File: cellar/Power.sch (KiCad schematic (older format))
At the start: 29 parts

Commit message: Schematic done, pending review.
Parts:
- removed C? (x2): 22uF/6.3V, symbol Device:C
- added C14, C15: 22uF/6.3V, symbol Device:CP
- added MH1, MH2, MH3, MH4: MountingHole_Pad, MountingHole:MountingHole_3.2mm_M3_Pad_Via, symbol Mechanical:MountingHole_Pad
- D1, D2, D3: renamed from D?; Farnell (none) -> 1863724; Ref (none) -> SBR160S23-7
- R2: renamed from R?; value 37.4k -> 22.1k
- gave numbers to parts that had none: 23
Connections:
- wire segments 103 -> 112

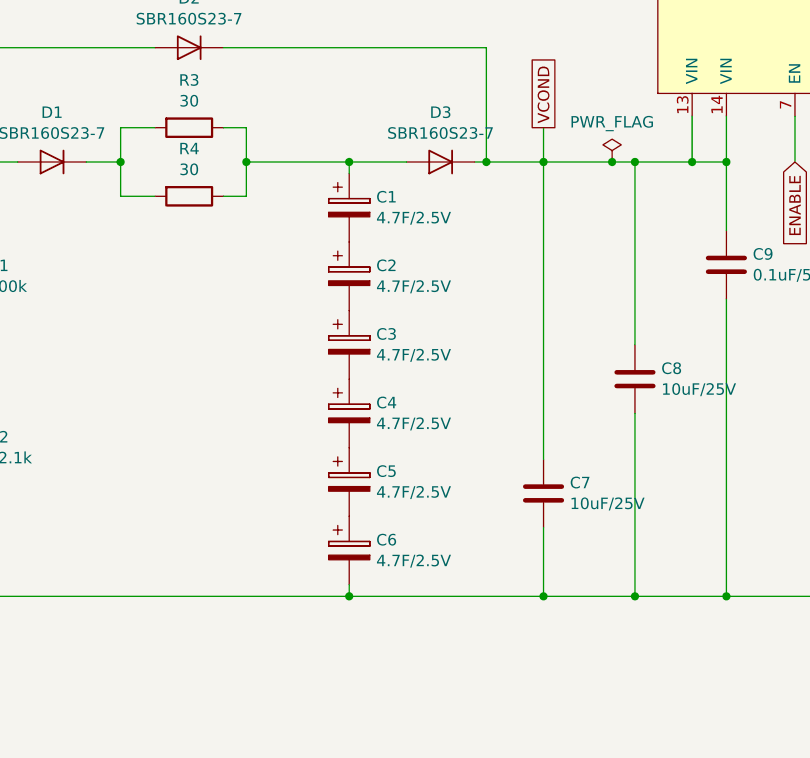
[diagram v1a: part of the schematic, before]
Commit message: Changed supercap ref, updated some footprints.
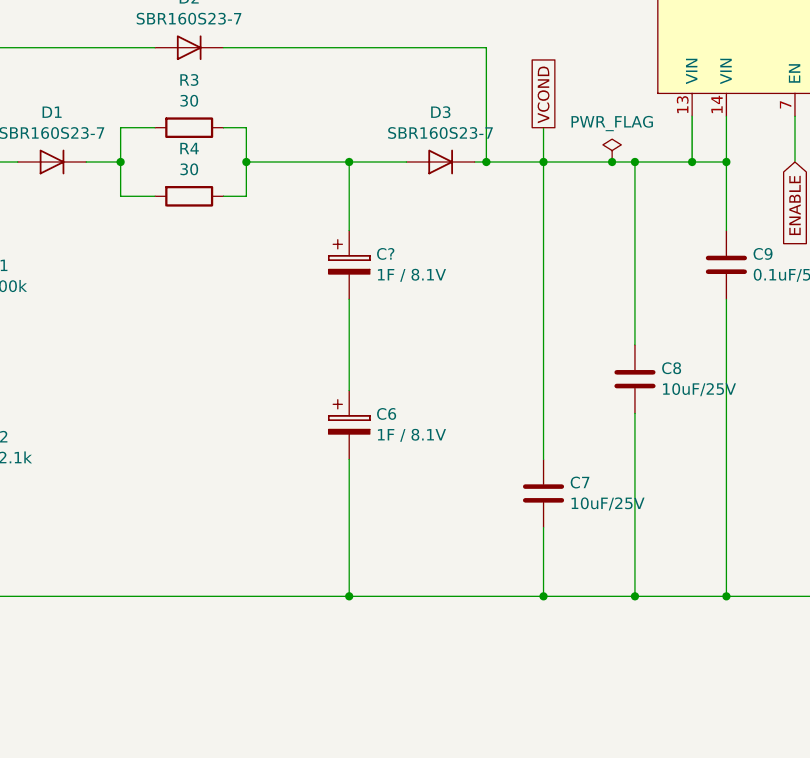
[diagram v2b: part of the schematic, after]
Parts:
- removed C1, C2, C3, C4, C5: 4.7F/2.5V, symbol Device:CP
- added C?: 1F / 8.1V, Capacitors:SCMR22J105SRBA0_vertical, symbol Device:CP
- C6: value 4.7F/2.5V -> 1F / 8.1V; footprint (none) -> Capacitors:SCMR22J105SRBA0_vertical; Farnell (none) -> 2856949; Ref (none) -> SCMR22J105SRBA0
- L1: footprint (none) -> Inductors:L_7.1x6.5_H3; Farnell (none) -> 2215610; Ref (none) -> SPM6530T-1R5M100
- R3, R4: Farnell (none) -> 2331667; Ref (none) -> SMW530RJT
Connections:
- wire segments 112 -> 113
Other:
- moved on the sheet: C6
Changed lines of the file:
@@
 F 0 "L1" H 8850 2315 50  0000 C CNN
 F 1 "1.5uH" H 8850 2224 50  0000 C CNN
-F 2 "" H 8850 2100 50  0001 C CNN
+F 2 "Inductors:L_7.1x6.5_H3" H 8850 2100 50  0001 C CNN
 F 3 "" H 8850 2100 50  0001 C CNN
+F 4 "2215610" H 8850 2100 50  0001 C CNN "Farnell"
+F 5 "SPM6530T-1R5M100" H 8850 2100 50  0001 C CNN "Ref"
 	1    8850 2100
 	1    0    0    -1
@@
 	10000 3600 10000 3750
 $Comp
-L Device:CP C1
-U 1 1 5BCFB2DD
-P 3750 1900
-F 0 "C1" H 3868 1946 50  0000 L CNN
-F 1 "4.7F/2.5V" H 3868 1855 50  0000 L CNN
-F 2 "" H 3788 1750 50  0001 C CNN
-F 3 "~" H 3750 1900 50  0001 C CNN
-	1    3750 1900
-	1    0    0    -1
-$EndComp
-$Comp
-L Device:CP C2
-U 1 1 5BCFB408
-P 3750 2200
-F 0 "C2" H 3868 2246 50  0000 L CNN
-F 1 "4.7F/2.5V" H 3868 2155 50  0000 L CNN
-F 2 "" H 3788 2050 50  0001 C CNN
-F 3 "~" H 3750 2200 50  0001 C CNN
-	1    3750 2200
-	1    0    0    -1
-$EndComp
-$Comp
-L Device:CP C3
-U 1 1 5BCFB550
-P 3750 2500
-F 0 "C3" H 3868 2546 50  0000 L CNN
-F 1 "4.7F/2.5V" H 3868 2455 50  0000 L CNN
-F 2 "" H 3788 2350 50  0001 C CNN
-F 3 "~" H 3750 2500 50  0001 C CNN
-	1    3750 2500
-	1    0    0    -1
-$EndComp
-$Comp
-L Device:CP C4
-U 1 1 5BCFB58E
-P 3750 2800
-F 0 "C4" H 3868 2846 50  0000 L CNN
-F 1 "4.7F/2.5V" H 3868 2755 50  0000 L CNN
-F 2 "" H 3788 2650 50  0001 C CNN
-F 3 "~" H 3750 2800 50  0001 C CNN
-	1    3750 2800
-	1    0    0    -1
-$EndComp
-$Comp
-L Device:CP C5
-U 1 1 5BCFB5CA
-P 3750 3100
-F 0 "C5" H 3868 3146 50  0000 L CNN
-F 1 "4.7F/2.5V" H 3868 3055 50  0000 L CNN
-F 2 "" H 3788 2950 50  0001 C CNN
-F 3 "~" H 3750 3100 50  0001 C CNN
-	1    3750 3100
-	1    0    0    -1
-$EndComp
-$Comp
 L Device:CP C6
 U 1 1 5BCFB957
-P 3750 3400
-F 0 "C6" H 3868 3446 50  0000 L CNN
-F 1 "4.7F/2.5V" H 3868 3355 50  0000 L CNN
-F 2 "" H 3788 3250 50  0001 C CNN
-F 3 "~" H 3750 3400 50  0001 C CNN
-	1    3750 3400
+P 3750 2850
+F 0 "C6" H 3868 2896 50  0000 L CNN
+F 1 "1F / 8.1V" H 3868 2805 50  0000 L CNN
+F 2 "Capacitors:SCMR22J105SRBA0_vertical" H 3788 2700 50  0001 C CNN
+F 3 "~" H 3750 2850 50  0001 C CNN
+F 4 "2856949" H 3750 2850 50  0001 C CNN "Farnell"
+F 5 "SCMR22J105SRBA0" H 3750 2850 50  0001 C CNN "Ref"
+	1    3750 2850
 	1    0    0    -1
 $EndComp
@@
 F 2 "" V 2980 1550 50  0001 C CNN
 F 3 "~" H 3050 1550 50  0001 C CNN
+F 4 "2331667" H 3050 1550 50  0001 C CNN "Farnell"
+F 5 "SMW530RJT" H 3050 1550 50  0001 C CNN "Ref"
 	1    3050 1550
-	0    1    1    0
-$EndComp
-$Comp
-L Device:R R4
-U 1 1 5BCFCCFA
-P 3050 1850
-F 0 "R4" V 2843 1850 50  0000 C CNN
-F 1 "30" V 2934 1850 50  0000 C CNN
-F 2 "" V 2980 1850 50  0001 C CNN
-F 3 "~" H 3050 1850 50  0001 C CNN
-	1    3050 1850
 	0    1    1    0
 $EndComp
@@
 	4000 1700 3750 1700
 Wire Wire Line
-	3750 1700 3750 1750
-Wire Wire Line
-	3750 3550 3750 3600
+	3750 3000 3750 3600
 Wire Wire Line
 	3750 3600 4600 3600
@@
 Wire Wire Line
 	4900 1700 4600 1700
+$Comp
+L Device:R R4
+U 1 1 5BECFA96
+P 3050 1850
+F 0 "R4" V 2843 1850 50  0000 C CNN
+F 1 "30" V 2934 1850 50  0000 C CNN
+F 2 "" V 2980 1850 50  0001 C CNN
+F 3 "~" H 3050 1850 50  0001 C CNN
+F 4 "2331667" H 3050 1850 50  0001 C CNN "Farnell"
+F 5 "SMW530RJT" H 3050 1850 50  0001 C CNN "Ref"
+	1    3050 1850
+	0    1    1    0
+$EndComp
+$Comp
+L Device:CP C?
+U 1 1 5BED7949
+P 3750 2150
+F 0 "C?" H 3868 2196 50  0000 L CNN
+F 1 "1F / 8.1V" H 3868 2105 50  0000 L CNN
+F 2 "Capacitors:SCMR22J105SRBA0_vertical" H 3788 2000 50  0001 C CNN
+F 3 "~" H 3750 2150 50  0001 C CNN
+F 4 "2856949" H 3750 2150 50  0001 C CNN "Farnell"
+F 5 "SCMR22J105SRBA0" H 3750 2150 50  0001 C CNN "Ref"
+	1    3750 2150
+	1    0    0    -1
+$EndComp
+Wire Wire Line
+	3750 2300 3750 2700
+Wire Wire Line
+	3750 1700 3750 2000
 $EndSCHEMATC

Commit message: Replaced wirepads by phoenix connectors.
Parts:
- removed W1: POWER +, Pads:wirepad_hole_3x1.5mm, symbol pads:WirePad
- removed W2: GND, Pads:wirepad_hole_3x1.5mm, symbol pads:WirePad
- C10: renamed from C14; footprint (none) -> Capacitor_Tantalum_SMD:CP_EIA-3216-10_Kemet-I_Pad1.58x1.35mm_HandSolder
- C11: renamed from C15; footprint (none) -> Capacitor_Tantalum_SMD:CP_EIA-3216-10_Kemet-I_Pad1.58x1.35mm_HandSolder
- C3: renamed from C7; footprint (none) -> Capacitor_SMD:C_0805_2012Metric_Pad1.15x1.40mm_HandSolder
- C4: renamed from C8; footprint (none) -> Capacitor_SMD:C_0805_2012Metric_Pad1.15x1.40mm_HandSolder
- C5: renamed from C9; footprint (none) -> Capacitor_SMD:C_0603_1608Metric_Pad1.05x0.95mm_HandSolder
- C6: renamed from C10; footprint (none) -> Capacitor_SMD:C_0805_2012Metric_Pad1.15x1.40mm_HandSolder
- C7: renamed from C11; footprint (none) -> Capacitor_SMD:C_0603_1608Metric_Pad1.05x0.95mm_HandSolder
- C8: renamed from C12; footprint (none) -> Capacitor_SMD:C_0603_1608Metric_Pad1.05x0.95mm_HandSolder
- C9: renamed from C13; footprint (none) -> Capacitor_SMD:C_0603_1608Metric_Pad1.05x0.95mm_HandSolder
- U1: Farnell (none) -> 2361244; Ref (none) -> TPS54625PWP
- gave numbers to parts that had none: 1
- renumbered C6 to C2
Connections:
- wire segments 113 -> 106
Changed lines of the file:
@@
 F 2 "TexasInstruments:HTSSOP-14-PWP" H 6850 800 50  0001 C CNN
 F 3 "http://www.ti.com/lit/ds/symlink/tps54625.pdf" H 6850 800 50  0001 C CNN
+F 4 "2361244" H 6850 800 50  0001 C CNN "Farnell"
+F 5 "TPS54625PWP" H 6850 800 50  0001 C CNN "Ref"
 	1    6850 800
 	1    0    0    -1
 $EndComp
 $Comp
-L Device:C C9
+L Device:C C5
 U 1 1 5BCDE8A2
 P 5400 2150
-F 0 "C9" H 5515 2196 50  0000 L CNN
+F 0 "C5" H 5515 2196 50  0000 L CNN
 F 1 "0.1uF/50V" H 5515 2105 50  0000 L CNN
-F 2 "" H 5438 2000 50  0001 C CNN
+F 2 "Capacitor_SMD:C_0603_1608Metric_Pad1.05x0.95mm_HandSolder" H 5438 2000 50  0001 C CNN
 F 3 "~" H 5400 2150 50  0001 C CNN
 	1    5400 2150
@@
 $EndComp
 $Comp
-L Device:C C8
+L Device:C C4
 U 1 1 5BCDE8C0
 P 5000 2650
-F 0 "C8" H 5115 2696 50  0000 L CNN
+F 0 "C4" H 5115 2696 50  0000 L CNN
 F 1 "10uF/25V" H 5115 2605 50  0000 L CNN
-F 2 "" H 5038 2500 50  0001 C CNN
+F 2 "Capacitor_SMD:C_0805_2012Metric_Pad1.15x1.40mm_HandSolder" H 5038 2500 50  0001 C CNN
 F 3 "~" H 5000 2650 50  0001 C CNN
 	1    5000 2650
@@
 $EndComp
 $Comp
-L Device:C C7
+L Device:C C3
 U 1 1 5BCDE8FA
 P 4600 3150
-F 0 "C7" H 4715 3196 50  0000 L CNN
+F 0 "C3" H 4715 3196 50  0000 L CNN
 F 1 "10uF/25V" H 4715 3105 50  0000 L CNN
-F 2 "" H 4638 3000 50  0001 C CNN
+F 2 "Capacitor_SMD:C_0805_2012Metric_Pad1.15x1.40mm_HandSolder" H 4638 3000 50  0001 C CNN
 F 3 "~" H 4600 3150 50  0001 C CNN
 	1    4600 3150
@@
 $EndComp
 $Comp
-L power:GND #PWR09
+L power:GND #PWR011
 U 1 1 5BCDE96A
 P 7050 3750
-F 0 "#PWR09" H 7050 3500 50  0001 C CNN
+F 0 "#PWR011" H 7050 3500 50  0001 C CNN
 F 1 "GND" H 7055 3577 50  0000 C CNN
 F 2 "" H 7050 3750 50  0001 C CNN
@@
 	5000 1700 5000 2500
 Connection ~ 5250 1700
-Wire Wire Line
-	5000 1700 4900 1700
 Wire Wire Line
 	4600 1700 4600 3000
@@
 $EndComp
 $Comp
-L Device:C C10
+L Device:C C6
 U 1 1 5BCDF240
 P 6150 2700
-F 0 "C10" H 6265 2746 50  0000 L CNN
+F 0 "C6" H 6265 2746 50  0000 L CNN
 F 1 "1uF/25V" H 6265 2655 50  0000 L CNN
-F 2 "" H 6188 2550 50  0001 C CNN
+F 2 "Capacitor_SMD:C_0805_2012Metric_Pad1.15x1.40mm_HandSolder" H 6188 2550 50  0001 C CNN
 F 3 "~" H 6150 2700 50  0001 C CNN
 	1    6150 2700
@@
 $EndComp
 $Comp
-L Device:C C11
+L Device:C C7
 U 1 1 5BCDF284
 P 6450 3200
-F 0 "C11" H 6565 3246 50  0000 L CNN
+F 0 "C7" H 6565 3246 50  0000 L CNN
 F 1 "8200pF/50V" H 6565 3155 50  0000 L CNN
-F 2 "" H 6488 3050 50  0001 C CNN
+F 2 "Capacitor_SMD:C_0603_1608Metric_Pad1.05x0.95mm_HandSolder" H 6488 3050 50  0001 C CNN
 F 3 "~" H 6450 3200 50  0001 C CNN
 	1    6450 3200
@@
 	6450 3600 7050 3600
 $Comp
-L Device:C C12
+L Device:C C8
 U 1 1 5BCE0D07
 P 7950 1750
-F 0 "C12" H 8065 1796 50  0000 L CNN
+F 0 "C8" H 8065 1796 50  0000 L CNN
 F 1 "0.1uF/50V" H 8065 1705 50  0000 L CNN
-F 2 "" H 7988 1600 50  0001 C CNN
+F 2 "Capacitor_SMD:C_0603_1608Metric_Pad1.05x0.95mm_HandSolder" H 7988 1600 50  0001 C CNN
 F 3 "~" H 7950 1750 50  0001 C CNN
 	1    7950 1750
@@
 $EndComp
 $Comp
-L Device:C C13
+L Device:C C9
 U 1 1 5BCE25CA
 P 8150 2600
-F 0 "C13" H 8265 2646 50  0000 L CNN
+F 0 "C9" H 8265 2646 50  0000 L CNN
 F 1 "10pF/50V" H 8265 2555 50  0000 L CNN
-F 2 "" H 8188 2450 50  0001 C CNN
+F 2 "Capacitor_SMD:C_0603_1608Metric_Pad1.05x0.95mm_HandSolder" H 8188 2450 50  0001 C CNN
 F 3 "~" H 8150 2600 50  0001 C CNN
 	1    8150 2600
@@
 	7050 3600 7050 3750
 $Comp
-L power:+5V #PWR011
+L power:+5V #PWR013
 U 1 1 5BCEEFBC
 P 10250 1850
-F 0 "#PWR011" H 10250 1700 50  0001 C CNN
+F 0 "#PWR013" H 10250 1700 50  0001 C CNN
 F 1 "+5V" H 10265 2023 50  0000 C CNN
 F 2 "" H 10250 1850 50  0001 C CNN
@@
 $EndComp
 $Comp
-L power:GND #PWR010
+L power:GND #PWR012
 U 1 1 5BCEF139
 P 10000 3750
-F 0 "#PWR010" H 10000 3500 50  0001 C CNN
+F 0 "#PWR012" H 10000 3500 50  0001 C CNN
 F 1 "GND" H 10005 3577 50  0000 C CNN
 F 2 "" H 10000 3750 50  0001 C CNN
@@
 $EndComp
 $Comp
-L power:GND #PWR07
+L power:GND #PWR09
 U 1 1 5BCEF24E
 P 2100 3750
-F 0 "#PWR07" H 2100 3500 50  0001 C CNN
+F 0 "#PWR09" H 2100 3500 50  0001 C CNN
 F 1 "GND" H 2105 3577 50  0000 C CNN
 F 2 "" H 2100 3750 50  0001 C CNN
@@
 	10000 3600 10000 3750
 $Comp
-L Device:CP C6
+L Device:CP C2
 U 1 1 5BCFB957
 P 3750 2850
-F 0 "C6" H 3868 2896 50  0000 L CNN
+F 0 "C2" H 3868 2896 50  0000 L CNN
 F 1 "1F / 8.1V" H 3868 2805 50  0000 L CNN
 F 2 "Capacitors:SCMR22J105SRBA0_vertical" H 3788 2700 50  0001 C CNN
@@
 	2100 2350 2100 2600
 $Comp
-L power:+12V #PWR06
+L power:+12V #PWR08
 U 1 1 5BD2D830
 P 1800 1450
-F 0 "#PWR06" H 1800 1300 50  0001 C CNN
+F 0 "#PWR08" H 1800 1300 50  0001 C CNN
 F 1 "+12V" H 1815 1623 50  0000 C CNN
 F 2 "" H 1800 1450 50  0001 C CNN
@@
 $EndComp
 Connection ~ 2100 3600
-$Comp
-L pads:WirePad W1
-U 1 1 5BD42CBA
-P 1100 6250
-F 0 "W1" V 885 6181 50  0000 C CNN
-F 1 "POWER +" V 976 6181 50  0000 C CNN
-F 2 "Pads:wirepad_hole_3x1.5mm" H 1100 6250 50  0001 C CNN
-F 3 "" H 1100 6250 50  0001 C CNN
-	1    1100 6250
-	0    1    1    0
-$EndComp
-$Comp
-L pads:WirePad W2
-U 1 1 5BD42E4B
-P 1100 6700
-F 0 "W2" V 885 6631 50  0000 C CNN
-F 1 "GND" V 976 6631 50  0000 C CNN
-F 2 "Pads:wirepad_hole_3x1.5mm" H 1100 6700 50  0001 C CNN
-F 3 "" H 1100 6700 50  0001 C CNN
-	1    1100 6700
-	0    1    1    0
-$EndComp
-Wire Wire Line
-	1100 6250 1350 6250
-Wire Wire Line
-	1600 6250 1600 5950
-Wire Wire Line
-	1100 6700 1350 6700
-Wire Wire Line
-	1600 6700 1600 7000
-$Comp
-L power:+12V #PWR04
-U 1 1 5BD48DD8
-P 1600 5950
-F 0 "#PWR04" H 1600 5800 50  0001 C CNN
-F 1 "+12V" H 1615 6123 50  0000 C CNN
-F 2 "" H 1600 5950 50  0001 C CNN
-F 3 "" H 1600 5950 50  0001 C CNN
-	1    1600 5950
-	1    0    0    -1
-$EndComp
-$Comp
-L power:GND #PWR05
-U 1 1 5BD48E3B
-P 1600 7000
-F 0 "#PWR05" H 1600 6750 50  0001 C CNN
-F 1 "GND" H 1605 6827 50  0000 C CNN
-F 2 "" H 1600 7000 50  0001 C CNN
-F 3 "" H 1600 7000 50  0001 C CNN
-	1    1600 7000
-	1    0    0    -1
-$EndComp
 Connection ~ 4350 1700
 Wire Wire Line
@@
 	3850 6900 3850 7100
 $Comp
-L power:GND #PWR08
+L power:GND #PWR010
 U 1 1 5BE43A97
 P 3850 7100
-F 0 "#PWR08" H 3850 6850 50  0001 C CNN
+F 0 "#PWR010" H 3850 6850 50  0001 C CNN
 F 1 "GND" H 3855 6927 50  0000 C CNN
 F 2 "" H 3850 7100 50  0001 C CNN
@@
 P 9450 3100
 AR Path="/5BE442FC/5BE47BD7" Ref="C?"  Part="1"
-AR Path="/5BCDDEA3/5BE47BD7" Ref="C14"  Part="1"
-F 0 "C14" H 9568 3146 50  0000 L CNN
+AR Path="/5BCDDEA3/5BE47BD7" Ref="C10"  Part="1"
+F 0 "C10" H 9568 3146 50  0000 L CNN
 F 1 "22uF/6.3V" H 9568 3055 50  0000 L CNN
-F 2 "" H 9488 2950 50  0001 C CNN
+F 2 "Capacitor_Tantalum_SMD:CP_EIA-3216-10_Kemet-I_Pad1.58x1.35mm_HandSolder" H 9488 2950 50  0001 C CNN
 F 3 "~" H 9450 3100 50  0001 C CNN
 F 4 "2321204" H 150 -300 50  0001 C CNN "Farnell"
@@
 P 10000 2600
 AR Path="/5BE442FC/5BE4EA38" Ref="C?"  Part="1"
-AR Path="/5BCDDEA3/5BE4EA38" Ref="C15"  Part="1"
-F 0 "C15" H 10118 2646 50  0000 L CNN
+AR Path="/5BCDDEA3/5BE4EA38" Ref="C11"  Part="1"
+F 0 "C11" H 10118 2646 50  0000 L CNN
 F 1 "22uF/6.3V" H 10118 2555 50  0000 L CNN
-F 2 "" H 10038 2450 50  0001 C CNN
+F 2 "Capacitor_Tantalum_SMD:CP_EIA-3216-10_Kemet-I_Pad1.58x1.35mm_HandSolder" H 10038 2450 50  0001 C CNN
 F 3 "~" H 10000 2600 50  0001 C CNN
 F 4 "2321204" H 700 -800 50  0001 C CNN "Farnell"
@@
 Text GLabel 5700 1700 3    50   Input ~ 0
 ENABLE
-$Comp
-L power:PWR_FLAG #FLG0102
-U 1 1 5BE87EF0
-P 1350 6250
-F 0 "#FLG0102" H 1350 6325 50  0001 C CNN
-F 1 "PWR_FLAG" H 1350 6424 50  0000 C CNN
-F 2 "" H 1350 6250 50  0001 C CNN
-F 3 "~" H 1350 6250 50  0001 C CNN
-	1    1350 6250
-	1    0    0    -1
-$EndComp
-Connection ~ 1350 6250
-Wire Wire Line
-	1350 6250 1600 6250
-$Comp
-L power:PWR_FLAG #FLG0103
-U 1 1 5BE87F46
-P 1350 6700
-F 0 "#FLG0103" H 1350 6775 50  0001 C CNN
-F 1 "PWR_FLAG" H 1350 6874 50  0000 C CNN
-F 2 "" H 1350 6700 50  0001 C CNN
-F 3 "~" H 1350 6700 50  0001 C CNN
-	1    1350 6700
-	1    0    0    -1
-$EndComp
-Connection ~ 1350 6700
-Wire Wire Line
-	1350 6700 1600 6700
 Wire Wire Line
 	9450 2100 10000 2100
 $Comp
-L power:PWR_FLAG #FLG0104
+L power:PWR_FLAG #FLG04
 U 1 1 5BE90F84
-P 4900 1700
-F 0 "#FLG0104" H 4900 1775 50  0001 C CNN
-F 1 "PWR_FLAG" H 4900 1874 50  0000 C CNN
-F 2 "" H 4900 1700 50  0001 C CNN
-F 3 "~" H 4900 1700 50  0001 C CNN
-	1    4900 1700
-	1    0    0    -1
-$EndComp
-Connection ~ 4900 1700
-Wire Wire Line
-	4900 1700 4600 1700
+P 5000 1700
+F 0 "#FLG04" H 5000 1775 50  0001 C CNN
+F 1 "PWR_FLAG" H 5000 1874 50  0000 C CNN
+F 2 "" H 5000 1700 50  0001 C CNN
+F 3 "~" H 5000 1700 50  0001 C CNN
+	1    5000 1700
+	1    0    0    -1
+$EndComp
 $Comp
 L Device:R R4
@@
 $EndComp
 $Comp
-L Device:CP C?
+L Device:CP C1
 U 1 1 5BED7949
 P 3750 2150
-F 0 "C?" H 3868 2196 50  0000 L CNN
+F 0 "C1" H 3868 2196 50  0000 L CNN
 F 1 "1F / 8.1V" H 3868 2105 50  0000 L CNN
 F 2 "Capacitors:SCMR22J105SRBA0_vertical" H 3788 2000 50  0001 C CNN
@@
 Wire Wire Line
 	3750 1700 3750 2000
+Wire Wire Line
+	4600 1700 5000 1700
 $EndSCHEMATC

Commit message: Routing in progress.
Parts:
- D1, D2, D3: footprint (none) -> Diode_SMD:D_SOT-23_ANK
- MH1, MH2, MH3, MH4: footprint MountingHole:MountingHole_3.2mm_M3_Pad_Via -> MountingHole:MountingHole_3.2mm_M3_DIN965
- R1, R2, R5, R6, R7: footprint (none) -> Resistor_SMD:R_0603_1608Metric_Pad1.05x0.95mm_HandSolder
- R3, R4: footprint (none) -> Resistors_custom:TE_SM5
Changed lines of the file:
@@
 F 0 "R5" H 6070 1996 50  0000 L CNN
 F 1 "100k" H 6070 1905 50  0000 L CNN
-F 2 "" V 5930 1950 50  0001 C CNN
+F 2 "Resistor_SMD:R_0603_1608Metric_Pad1.05x0.95mm_HandSolder" V 5930 1950 50  0001 C CNN
 F 3 "~" H 6000 1950 50  0001 C CNN
 	1    6000 1950
@@
 F 0 "R6" H 7720 2646 50  0000 L CNN
 F 1 "124k 1%" H 7720 2555 50  0000 L CNN
-F 2 "" V 7580 2600 50  0001 C CNN
+F 2 "Resistor_SMD:R_0603_1608Metric_Pad1.05x0.95mm_HandSolder" V 7580 2600 50  0001 C CNN
 F 3 "~" H 7650 2600 50  0001 C CNN
 	1    7650 2600
@@
 F 0 "R7" H 7720 3246 50  0000 L CNN
 F 1 "22.1k 1%" H 7720 3155 50  0000 L CNN
-F 2 "" V 7580 3200 50  0001 C CNN
+F 2 "Resistor_SMD:R_0603_1608Metric_Pad1.05x0.95mm_HandSolder" V 7580 3200 50  0001 C CNN
 F 3 "~" H 7650 3200 50  0001 C CNN
 	1    7650 3200
@@
 F 0 "D3" H 4150 1484 50  0000 C CNN
 F 1 "SBR160S23-7" H 4150 1575 50  0000 C CNN
-F 2 "" H 4150 1700 50  0001 C CNN
+F 2 "Diode_SMD:D_SOT-23_ANK" H 4150 1700 50  0001 C CNN
 F 3 "~" H 4150 1700 50  0001 C CNN
 F 4 "1863724" H 0   0   50  0001 C CNN "Farnell"
@@
 F 0 "D2" H 3050 984 50  0000 C CNN
 F 1 "SBR160S23-7" H 3050 1075 50  0000 C CNN
-F 2 "" H 3050 1200 50  0001 C CNN
+F 2 "Diode_SMD:D_SOT-23_ANK" H 3050 1200 50  0001 C CNN
 F 3 "~" H 3050 1200 50  0001 C CNN
 F 4 "1863724" H 0   0   50  0001 C CNN "Farnell"
@@
 F 0 "R3" V 2843 1550 50  0000 C CNN
 F 1 "30" V 2934 1550 50  0000 C CNN
-F 2 "" V 2980 1550 50  0001 C CNN
+F 2 "Resistors_custom:TE_SM5" V 2980 1550 50  0001 C CNN
 F 3 "~" H 3050 1550 50  0001 C CNN
 F 4 "2331667" H 3050 1550 50  0001 C CNN "Farnell"
@@
 F 0 "D1" H 2450 1484 50  0000 C CNN
 F 1 "SBR160S23-7" H 2450 1575 50  0000 C CNN
-F 2 "" H 2450 1700 50  0001 C CNN
+F 2 "Diode_SMD:D_SOT-23_ANK" H 2450 1700 50  0001 C CNN
 F 3 "~" H 2450 1700 50  0001 C CNN
 F 4 "1863724" H 0   0   50  0001 C CNN "Farnell"
@@
 F 0 "R1" H 2170 2246 50  0000 L CNN
 F 1 "100k" H 2170 2155 50  0000 L CNN
-F 2 "" V 2030 2200 50  0001 C CNN
+F 2 "Resistor_SMD:R_0603_1608Metric_Pad1.05x0.95mm_HandSolder" V 2030 2200 50  0001 C CNN
 F 3 "~" H 2100 2200 50  0001 C CNN
 	1    2100 2200
@@
 F 0 "R2" H 2170 2996 50  0000 L CNN
 F 1 "22.1k" H 2170 2905 50  0000 L CNN
-F 2 "" V 2030 2950 50  0001 C CNN
+F 2 "Resistor_SMD:R_0603_1608Metric_Pad1.05x0.95mm_HandSolder" V 2030 2950 50  0001 C CNN
 F 3 "~" H 2100 2950 50  0001 C CNN
 	1    2100 2950
@@
 F 0 "MH1" V 3637 6455 50  0000 C CNN
 F 1 "MountingHole_Pad" V 3546 6455 50  0000 C CNN
-F 2 "MountingHole:MountingHole_3.2mm_M3_Pad_Via" H 3400 6450 50  0001 C CNN
+F 2 "MountingHole:MountingHole_3.2mm_M3_DIN965" H 3400 6450 50  0001 C CNN
 F 3 "~" H 3400 6450 50  0001 C CNN
 	1    3400 6450
@@
 	1    3850 7100
 	1    0    0    -1
-$EndComp
-$Comp
-L Mechanical:MountingHole_Pad MH2
-U 1 1 5BE43C16
-P 3400 6900
-F 0 "MH2" V 3637 6905 50  0000 C CNN
-F 1 "MountingHole_Pad" V 3546 6905 50  0000 C CNN
-F 2 "MountingHole:MountingHole_3.2mm_M3_Pad_Via" H 3400 6900 50  0001 C CNN
-F 3 "~" H 3400 6900 50  0001 C CNN
-	1    3400 6900
-	0    -1   -1   0
-$EndComp
-$Comp
-L Mechanical:MountingHole_Pad MH3
-U 1 1 5BE43C6E
-P 4300 6450
-F 0 "MH3" V 4254 6600 50  0000 L CNN
-F 1 "MountingHole_Pad" V 4345 6600 50  0000 L CNN
-F 2 "MountingHole:MountingHole_3.2mm_M3_Pad_Via" H 4300 6450 50  0001 C CNN
-F 3 "~" H 4300 6450 50  0001 C CNN
-	1    4300 6450
-	0    1    1    0
-$EndComp
-$Comp
-L Mechanical:MountingHole_Pad MH4
-U 1 1 5BE43D16
-P 4300 6900
-F 0 "MH4" V 4254 7050 50  0000 L CNN
-F 1 "MountingHole_Pad" V 4345 7050 50  0000 L CNN
-F 2 "MountingHole:MountingHole_3.2mm_M3_Pad_Via" H 4300 6900 50  0001 C CNN
-F 3 "~" H 4300 6900 50  0001 C CNN
-	1    4300 6900
-	0    1    1    0
 $EndComp
 $Comp
@@
 F 0 "R4" V 2843 1850 50  0000 C CNN
 F 1 "30" V 2934 1850 50  0000 C CNN
-F 2 "" V 2980 1850 50  0001 C CNN
+F 2 "Resistors_custom:TE_SM5" V 2980 1850 50  0001 C CNN
 F 3 "~" H 3050 1850 50  0001 C CNN
 F 4 "2331667" H 3050 1850 50  0001 C CNN "Farnell"
@@
 Wire Wire Line
 	4600 1700 5000 1700
+$Comp
+L Mechanical:MountingHole_Pad MH2
+U 1 1 5BECA8ED
+P 3400 6900
+F 0 "MH2" V 3637 6905 50  0000 C CNN
+F 1 "MountingHole_Pad" V 3546 6905 50  0000 C CNN
+F 2 "MountingHole:MountingHole_3.2mm_M3_DIN965" H 3400 6900 50  0001 C CNN
+F 3 "~" H 3400 6900 50  0001 C CNN
+	1    3400 6900
+	0    -1   -1   0
+$EndComp
+$Comp
+L Mechanical:MountingHole_Pad MH3
+U 1 1 5BECA939
+P 4300 6450
+F 0 "MH3" V 4537 6455 50  0000 C CNN
+F 1 "MountingHole_Pad" V 4446 6455 50  0000 C CNN
+F 2 "MountingHole:MountingHole_3.2mm_M3_DIN965" H 4300 6450 50  0001 C CNN
+F 3 "~" H 4300 6450 50  0001 C CNN
+	1    4300 6450
+	0    1    1    0
+$EndComp
+$Comp
+L Mechanical:MountingHole_Pad MH4
+U 1 1 5BECA9BB
+P 4300 6900
+F 0 "MH4" V 4537 6905 50  0000 C CNN
+F 1 "MountingHole_Pad" V 4446 6905 50  0000 C CNN
+F 2 "MountingHole:MountingHole_3.2mm_M3_DIN965" H 4300 6900 50  0001 C CNN
+F 3 "~" H 4300 6900 50  0001 C CNN
+	1    4300 6900
+	0    1    1    0
+$EndComp
 $EndSCHEMATC
